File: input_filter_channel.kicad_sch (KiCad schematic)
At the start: 25 parts, among them K1 EC2-12TNU, U1 OPA1612AxD, U17 ADA4945-1, U9 OPA1612AxD

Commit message: Updated Schematics with recent changes
Made Updates with recent suggestions.
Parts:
- C? (x2): value 22nF -> 22uF
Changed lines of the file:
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@@
       (effects (font (size 1.27 1.27)) (justify left))
     )
-    (property "Value" "22nF" (at 208.28 134.62 90)
+    (property "Value" "22uF" (at 208.28 134.62 90)
       (effects (font (size 1.27 1.27)) (justify left))
     )
@@
       (effects (font (size 1.27 1.27)) (justify left))
     )
-    (property "Value" "22nF" (at 208.28 144.78 90)
+    (property "Value" "22uF" (at 208.28 144.78 90)
       (effects (font (size 1.27 1.27)) (justify left))
     )

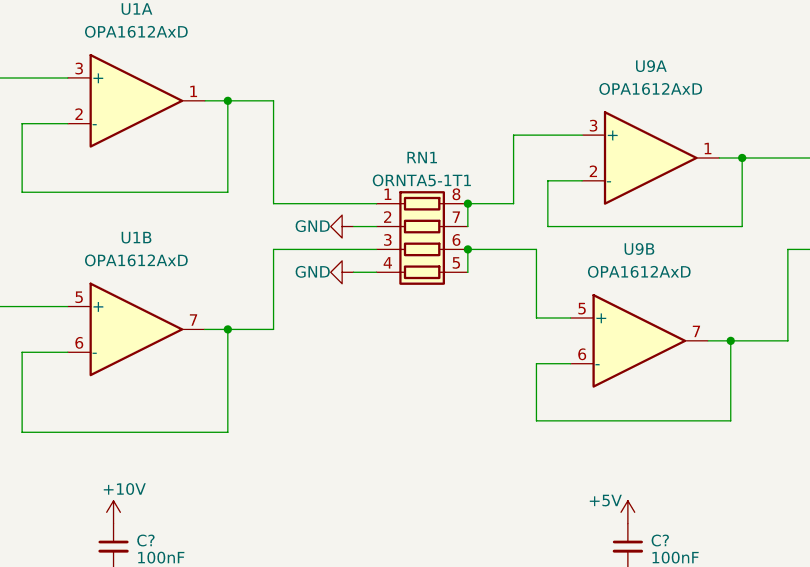
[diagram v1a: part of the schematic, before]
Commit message: Updated Channel 1 and fixes from review
Updated Channel 1 to use the INA851.
Fixed the ORNTA part pinout.
Fixed feedback on LT1763s.
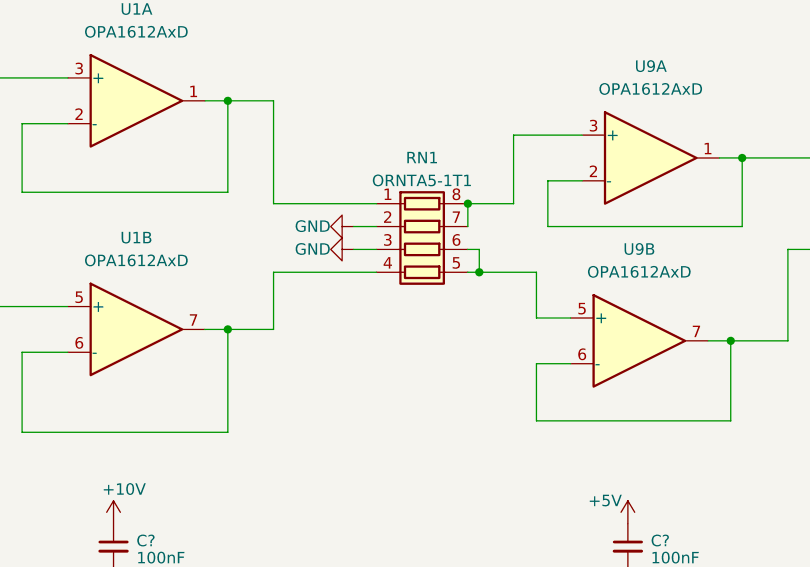
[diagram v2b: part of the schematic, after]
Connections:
- net GND: now also RN1.3 (R3.1); no longer RN1.4 (R4.1)
- net at U1.6 (-), U1.7: now also RN1.4 (R4.1); no longer RN1.3 (R3.1)
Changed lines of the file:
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@@
   (junction (at 208.28 138.43) (diameter 0) (color 0 0 0 0)
   )
-  (junction (at 165.1 138.43) (diameter 0) (color 0 0 0 0)
-  )
   (junction (at 288.29 140.97) (diameter 0) (color 0 0 0 0)
   )
@@
   (junction (at 337.82 110.49) (diameter 0) (color 0 0 0 0)
   )
+  (junction (at 166.37 140.97) (diameter 0) (color 0 0 0 0)
+  )
   (junction (at 295.91 199.39) (diameter 0) (color 0 0 0 0)
   )
@@
     (stroke (width 0) (type default))
   )
+  (wire (pts (xy 166.37 140.97) (xy 172.72 140.97))
+    (stroke (width 0) (type default))
+  )
   (wire (pts (xy 260.35 140.97) (xy 288.29 140.97))
     (stroke (width 0) (type default))
@@
     (stroke (width 0) (type default))
   )
-  (wire (pts (xy 152.4 140.97) (xy 154.94 140.97))
+  (wire (pts (xy 152.4 138.43) (xy 154.94 138.43))
     (stroke (width 0) (type default))
   )
@@
     (stroke (width 0) (type default))
   )
-  (wire (pts (xy 172.72 146.05) (xy 172.72 138.43))
+  (wire (pts (xy 172.72 146.05) (xy 172.72 140.97))
     (stroke (width 0) (type default))
   )
@@
     (stroke (width 0) (type default))
   )
+  (wire (pts (xy 165.1 138.43) (xy 166.37 138.43))
+    (stroke (width 0) (type default))
+  )
   (wire (pts (xy 138.43 121.92) (xy 135.89 121.92))
     (stroke (width 0) (type default))
@@
     (stroke (width 0) (type default))
   )
-  (wire (pts (xy 172.72 138.43) (xy 165.1 138.43))
-    (stroke (width 0) (type default))
-  )
   (wire (pts (xy 173.99 130.81) (xy 173.99 135.89))
     (stroke (width 0) (type default))
@@
     (stroke (width 0) (type default))
   )
-  (wire (pts (xy 165.1 138.43) (xy 165.1 140.97))
-    (stroke (width 0) (type default))
-  )
   (wire (pts (xy 101.6 135.89) (xy 101.6 144.78))
     (stroke (width 0) (type default))
@@
     (stroke (width 0) (type default))
   )
+  (wire (pts (xy 143.51 140.97) (xy 154.94 140.97))
+    (stroke (width 0) (type default))
+  )
   (wire (pts (xy 326.39 133.35) (xy 326.39 125.73))
     (stroke (width 0) (type default))
@@
     (stroke (width 0) (type default))
   )
-  (wire (pts (xy 154.94 138.43) (xy 143.51 138.43))
+  (wire (pts (xy 300.99 143.51) (xy 300.99 148.59))
     (stroke (width 0) (type default))
   )
-  (wire (pts (xy 300.99 143.51) (xy 300.99 148.59))
+  (wire (pts (xy 166.37 138.43) (xy 166.37 140.97))
     (stroke (width 0) (type default))
   )
@@
     (stroke (width 0) (type default))
   )
+  (wire (pts (xy 165.1 140.97) (xy 166.37 140.97))
+    (stroke (width 0) (type default))
+  )
   (wire (pts (xy 300.99 175.26) (xy 300.99 176.53))
     (stroke (width 0) (type default))
@@
     (stroke (width 0) (type default))
   )
-  (wire (pts (xy 143.51 138.43) (xy 143.51 147.32))
-    (stroke (width 0) (type default))
-  )
   (wire (pts (xy 236.22 120.65) (xy 241.3 120.65))
     (stroke (width 0) (type default))
@@
     (stroke (width 0) (type default))
   )
+  (wire (pts (xy 143.51 140.97) (xy 143.51 147.32))
+    (stroke (width 0) (type default))
+  )
   (hierarchical_label "Relay_SetCoil" (shape input) (at 241.3 120.65 0) (fields_autoplaced)
     (effects (font (size 1.27 1.27)) (justify left))
@@
     )
   )
-  (symbol (lib_id "power:GND") (at 152.4 140.97 270) (unit 1)
+  (symbol (lib_id "power:GND") (at 152.4 138.43 270) (unit 1)
     (in_bom yes) (on_board yes) (dnp no)
-    (property "Reference" "#PWR?" (at 146.05 140.97 0)
+    (property "Reference" "#PWR?" (at 146.05 138.43 0)
       (effects (font (size 1.27 1.27)) hide)
     )
-    (property "Value" "GND" (at 149.86 140.97 90)
+    (property "Value" "GND" (at 149.86 138.43 90)
       (effects (font (size 1.27 1.27)) (justify right))
     )
-    (property "Footprint" "" (at 152.4 140.97 0)
+    (property "Footprint" "" (at 152.4 138.43 0)
       (effects (font (size 1.27 1.27)) hide)
     )
-    (property "Datasheet" "" (at 152.4 140.97 0)
+    (property "Datasheet" "" (at 152.4 138.43 0)
       (effects (font (size 1.27 1.27)) hide)
     )
